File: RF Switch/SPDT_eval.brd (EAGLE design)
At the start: 21.3 x 26.4 mm, 10 parts, among them J1 142-0711-821, J2 142-0711-821, J3 142-0711-821, J4 22-23-2051, U1 QPC1022

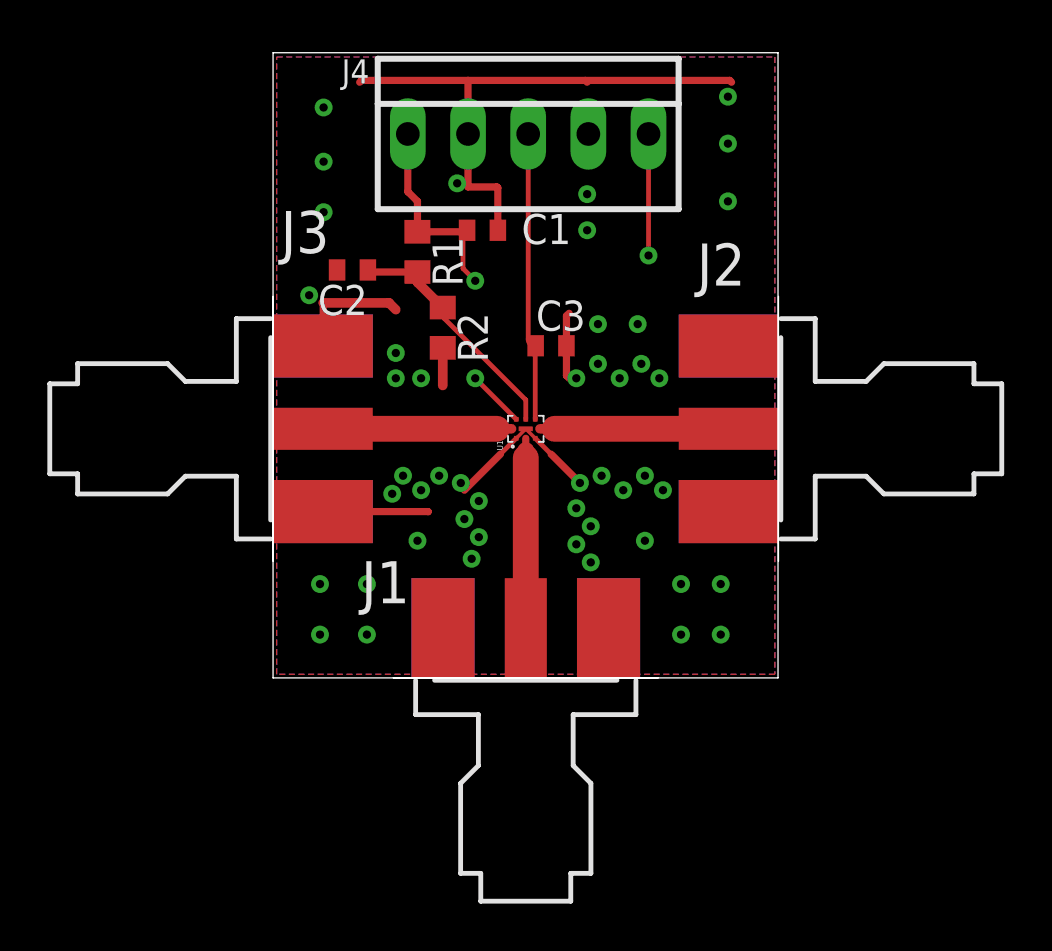
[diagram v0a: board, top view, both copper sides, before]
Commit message: Cleaned up SPDT switch evaluation board. Same as filter, cleaned up lots of EAGLE stuff. - 10 mil grid, snapped to grid. - Replaced SMA conectors - RF class added. - OSH park 2 layer (4 LAYER?!) DRC used. - Added frame and added names to signals. - Added board name.
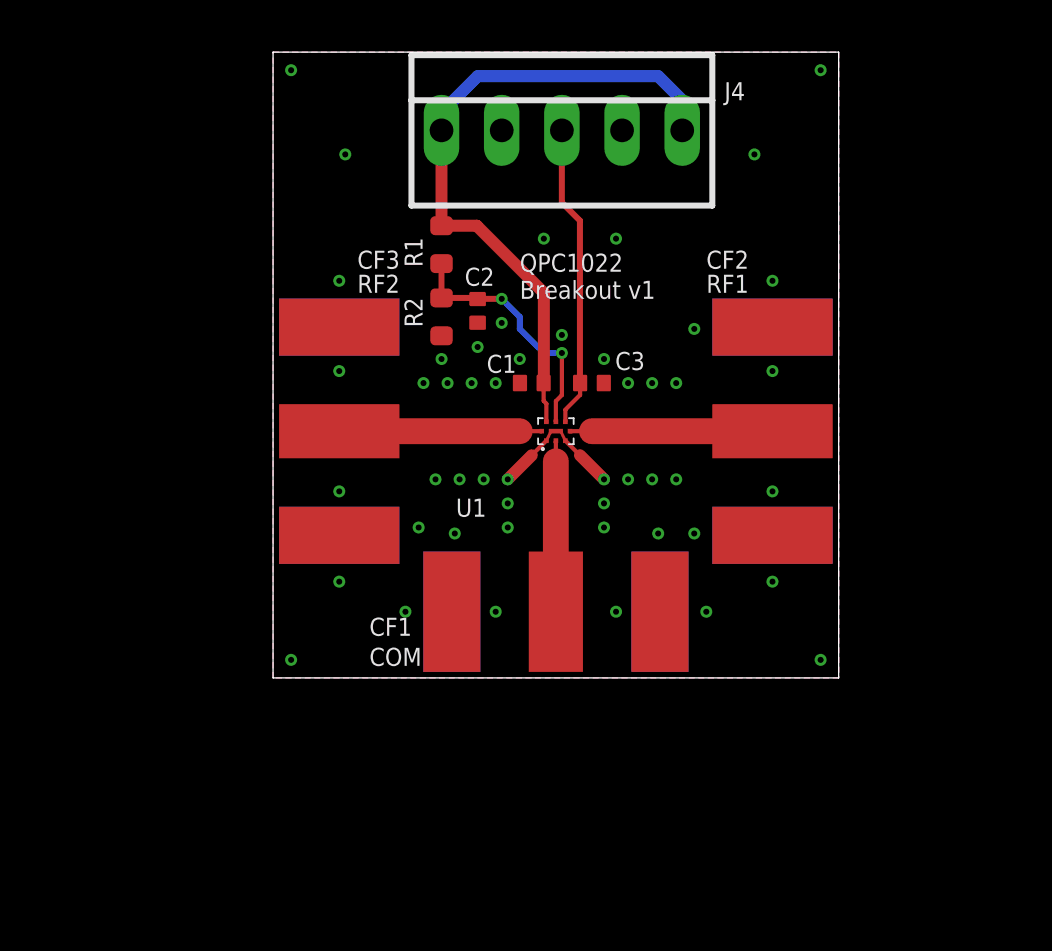
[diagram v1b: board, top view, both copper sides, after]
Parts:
- removed J1, J2, J3: 142-0711-821, con-coax:J502-ND-142-0711-821/826
- added CF1, CF2, CF3: SMA-CINCH-END-FIRE, psas_c3_team05:SMAJ716-ND
- C1: value (none) -> 2.2n; device rcl:C0402 -> rcl_custom:.0402-B-NOSILK
- C2, C3: value (none) -> 100p; device rcl:C0402 -> rcl_custom:.0402-B-NOSILK
- R1: value (none) -> 10k; device rcl:R0603 -> rcl_custom:.0603-B-NOSILK
- R2: value (none) -> 5.62k; device rcl:R0603 -> rcl_custom:.0603-B-NOSILK
- moved C1 6.78 mm to (10.9, 12.4), turned to 180 degrees
- moved C2 5.56 mm to (8.64, 15.5), turned to 270 degrees
- moved C3 2.34 mm to (13.5, 12.4)
- moved J4 1.43 mm to (12.2, 23.1)
- moved U1 1.27 mm to (11.9, 10.4)
- moved R1 1.06 mm to (7.11, 18.3)
- moved R2 0.46 mm to (7.11, 15.2)
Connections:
- net N$4 renamed VDD
- net N$5 renamed EN
- net N$7 renamed CTRL
- removed net N$1: J1.1, U1.ANT
- removed net N$2: J2.1, U1.RF1
- removed net N$3: J3.1, U1.RF2
- new net COM: CF1.P$3, U1.ANT
- new net RF1: CF2.P$3, U1.RF1
- new net RF2: CF3.P$3, U1.RF2
- net GND: now also CF1.GND1, CF1.GND2, CF1.GND3, CF1.GND4, CF2.GND1, CF2.GND2, CF2.GND3, CF2.GND4, CF3.GND1, CF3.GND2, CF3.GND3, CF3.GND4; no longer J1.G@1, J1.G@2, J1.G@3, J1.G@4, J2.G@1, J2.G@2, J2.G@3, J2.G@4, J3.G@1, J3.G@2, J3.G@3, J3.G@4
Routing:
- net GND: track 44.4 -> 5.91 mm, vias 48 -> 50
- net RF1: track 0.00 -> 8.54 mm
- net RF2: track 0.00 -> 8.54 mm
- net N$1: track 8.00 -> 0.00 mm
- net N$2: track 7.95 -> 0.00 mm
- net N$3: track 7.95 -> 0.00 mm
- net COM: track 0.00 -> 7.22 mm
- net EN: track 10.2 -> 11.1 mm, vias 0 -> 2
- net CTRL: track 12.2 -> 12.9 mm
- net VDD: track 28.2 -> 28.3 mm, vias 3 -> 0
- removed copper zone on layer 15, net GND
- removed copper zone on layer 2, net GND
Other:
- board size 21.3 x 26.4 mm -> 23.9 x 26.4 mm
- board text added: "COM"
- board text added: "QPC1022 Breakout v1"
- board text added: "RF1"
- board text added: "RF2"
